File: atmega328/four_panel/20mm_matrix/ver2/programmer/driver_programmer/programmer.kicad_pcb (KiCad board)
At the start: 2 copper layers, 40 x 80 mm, 8 parts, among them P0 CONN_2X2, P1 CONN_2X2, P2 CONN_2X2, P3 CONN_2X2, P4 CONN_3X2, P5 CONN_2

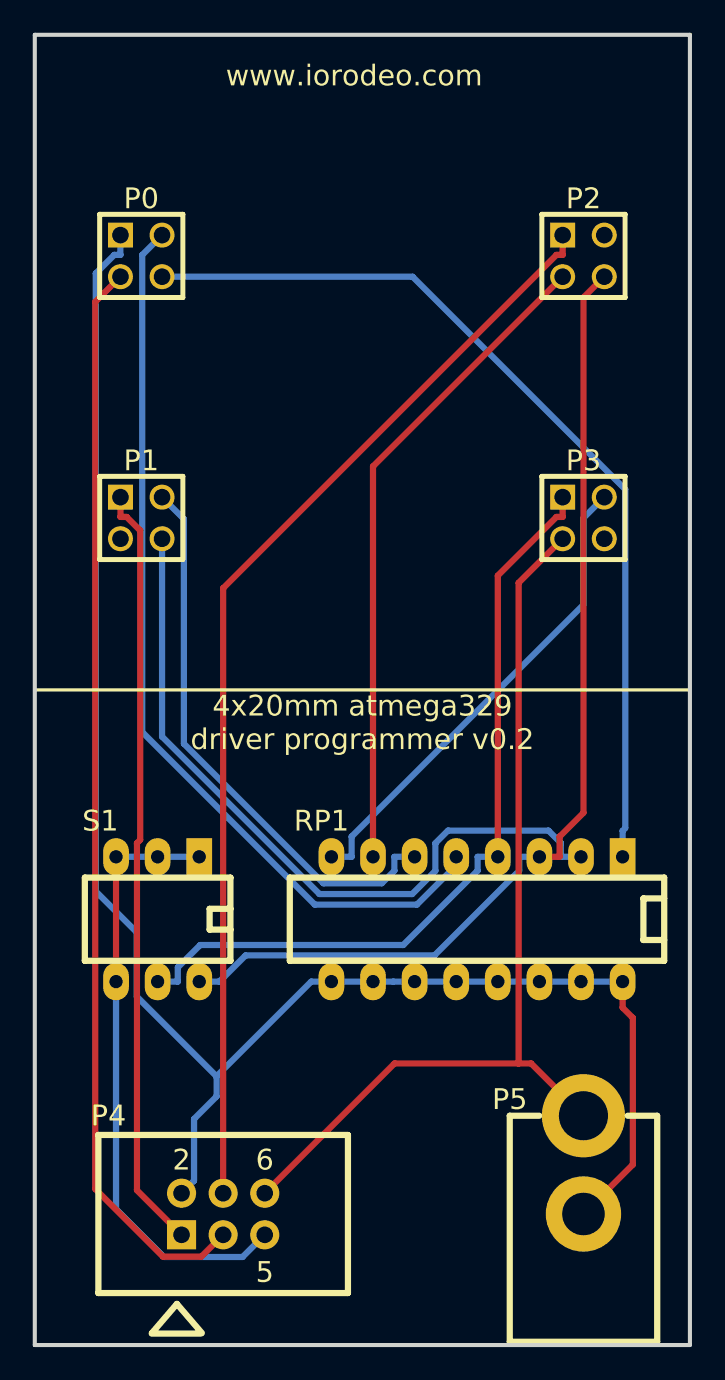
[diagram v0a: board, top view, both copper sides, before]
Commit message: Fixed error in v0.2 of atmega328 4x20mm driver programmer.
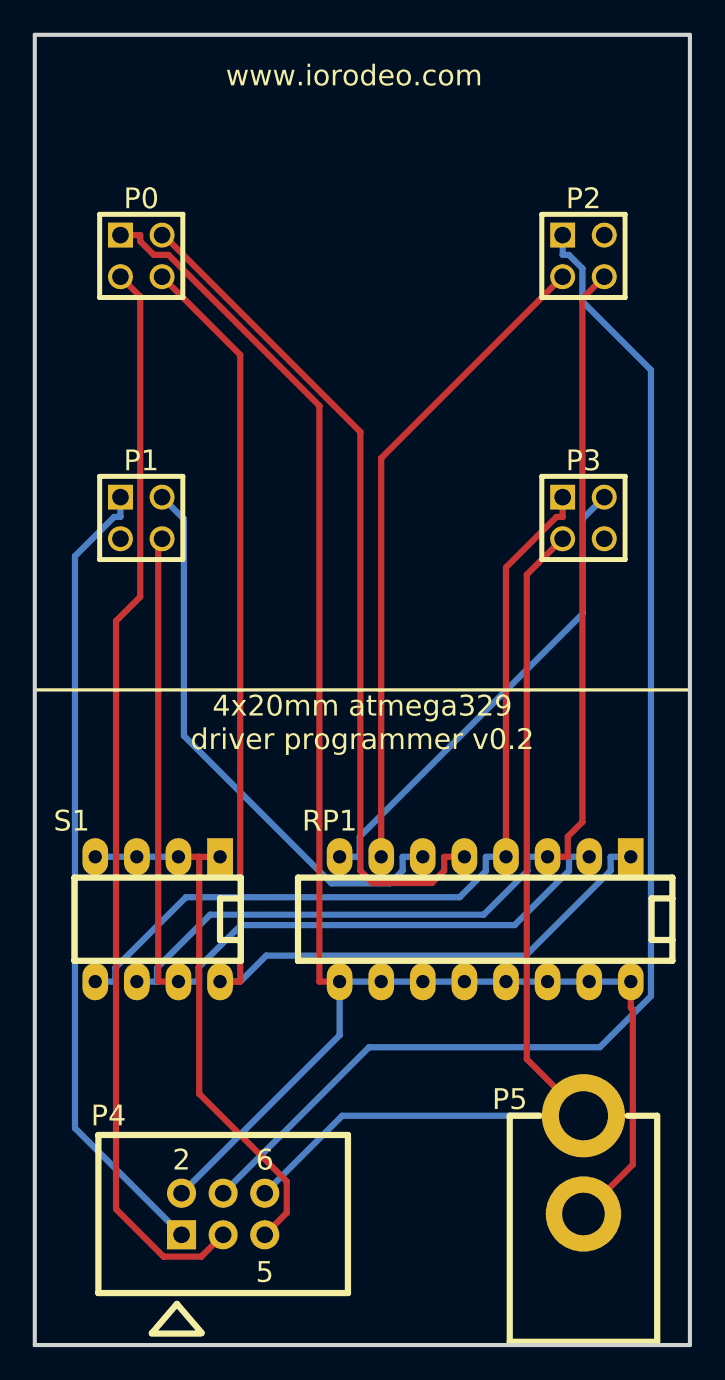
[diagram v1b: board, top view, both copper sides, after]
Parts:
- S1: footprint DIP-6__300_ELL -> DIP-8__300_ELL
- moved RP1 0.50 mm to (77.5, 104.0)
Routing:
- net /RESET_DRV0: track 56.2 -> 75.0 mm
- net /MOSI: track 67.3 -> 80.0 mm
- net /RESET_DRV1: track 45.4 -> 57.6 mm
- net /RESET_DRV2: track 62.2 -> 66.8 mm
- net /CS0: track 55.9 -> 51.7 mm
- net /RESET_DRV3: track 48.8 -> 52.9 mm
- net /RESET: track 37.4 -> 33.5 mm
- net +5V: track 106.2 -> 103.3 mm
- net /MISO: track 47.0 -> 49.1 mm
- net GND: track 57.2 -> 59.0 mm

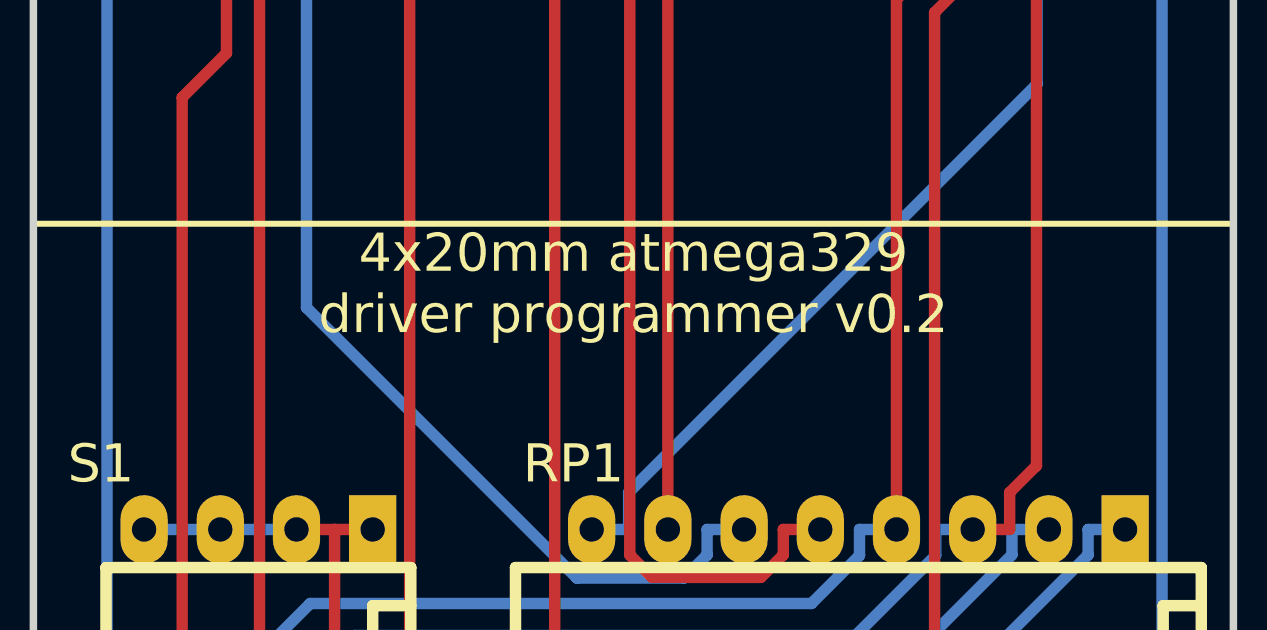
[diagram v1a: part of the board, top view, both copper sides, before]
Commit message: Modified version # text on PCB and created new set of gerber files.
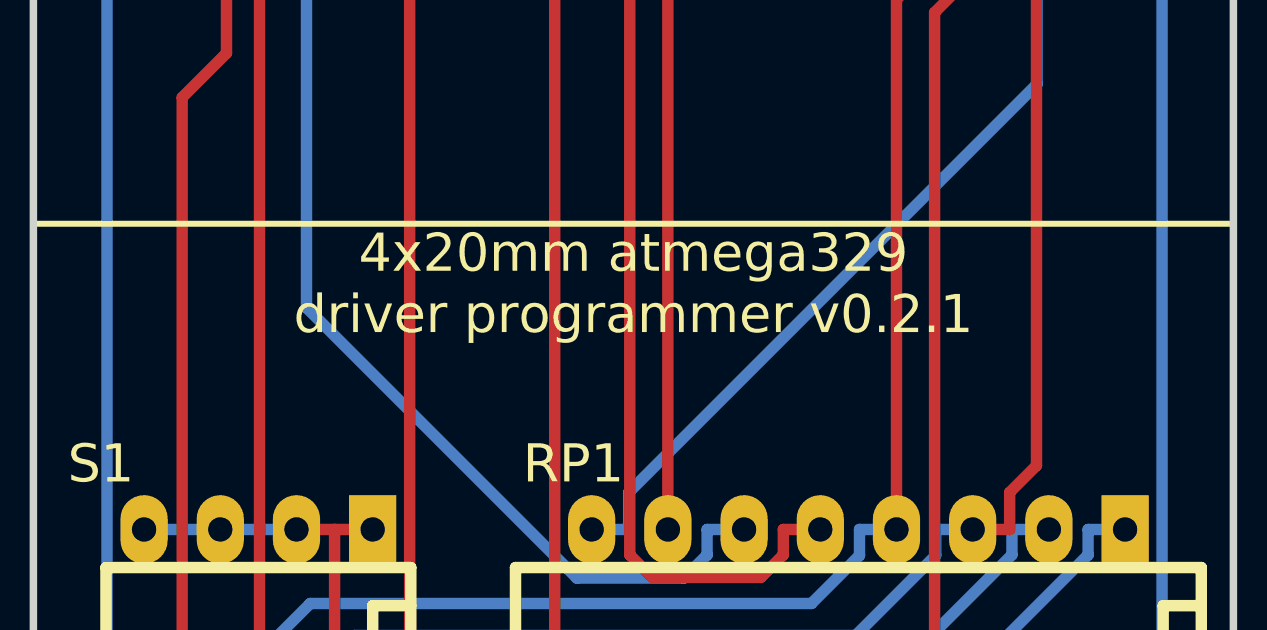
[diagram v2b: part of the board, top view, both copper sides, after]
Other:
- board text added: "4x20mm atmega329 driver programmer v0.2.1"
- board text removed: "4x20mm atmega329 driver programmer v0.2"
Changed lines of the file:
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@@
     (links 31)
     (no_connects 0)
-    (area 49.874999 49.874999 90.125001 130.125001)
+    (area 49.874999 49.874999 90.125001 130.244321)
     (thickness 1.6)
     (drawings 7)
@@
       (drillshape 0)
       (scaleselection 1)
-      (outputdirectory gerber_v0p2/))
+      (outputdirectory gerber_v0p21/))
   )
   (net 0 "")
@@
     (effects (font (size 1.27 1.27) (thickness 0.254)))
   )
-  (gr_text "4x20mm atmega329 \ndriver programmer v0.2" (at 70 92) (layer F.SilkS)
+  (gr_text "4x20mm atmega329 \ndriver programmer v0.2.1" (at 70 92) (layer F.SilkS)
     (effects (font (size 1.27 1.27) (thickness 0.254)))
   )
